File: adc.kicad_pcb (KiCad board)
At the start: 2 copper layers, 53.8 x 69.1 mm, 52 parts, among them J1 Conn_01x08_Male, J2 Conn_01x06_Male, J3 Conn_01x08_Male, J4 Conn_01x10_Male, J5 Conn_02x08_Odd_Even, J6 Conn_02x08_Odd_Even, J7 Conn_02x08_Odd_Even, U1 ADC128D818, U2 ADC128D818, U3 ADC128D818

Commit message: misc
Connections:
- J1 pad 8: 3V3 -> Net-(J1-Pad8)
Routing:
- net GND: track 32.3 -> 35.3 mm, vias 12 -> 7
- net SDA: track 70.2 -> 69.6 mm
- net Net-(R15-Pad1): track 20.2 -> 20.8 mm
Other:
- net class Default: clearance 0.2032 -> 0.1524; via_dia 0.4064 -> 0.508; via_drill 0.3556 -> 0.254
- net class Power: clearance 0.2032 -> 0.1524; via_dia 0.4064 -> 0.508; via_drill 0.3556 -> 0.254
- rule pad_to_mask_clearance: 0.051 -> 0.0508
- rule trace_clearance: 0.2032 -> 0.1524
- rule trace_min: 0.2 -> 0.1524
- rule via_min_drill: 0.3 -> 0.254
- rule via_min_size: 0.4 -> 0.508
- board text added: "0"
- board text added: "1"
- board text added: "2"
- board text added: "3"
- board text added: "4"
- board text added: "5"
- board text added: "6"
- board text added: "7"

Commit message: misc cleanup
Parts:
- moved R4 1.76 mm to (90.0, 73.2)
- moved R6 1.27 mm to (90.0, 76.8)
- moved R7 0.76 mm to (90.0, 80.5)
- moved R8 0.25 mm to (90.0, 84.2)
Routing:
- net 3V3: track 313.9 -> 317.6 mm
- net Net-(J5-Pad1): track 29.7 -> 32.1 mm
- net Net-(J5-Pad5): track 31.9 -> 34.3 mm
- net Net-(J5-Pad3): track 31.4 -> 33.5 mm
- net Net-(J7-Pad5): track 30.8 -> 32.2 mm
- net Net-(J7-Pad1): track 28.8 -> 30.1 mm
- net Net-(J6-Pad15): track 39.1 -> 40.3 mm
- net Net-(J5-Pad7): track 33.1 -> 34.2 mm
- net Net-(J6-Pad1): track 27.6 -> 28.7 mm
- net Net-(J7-Pad3): track 29.5 -> 30.3 mm
- net Net-(J5-Pad11): track 36.3 -> 35.7 mm
- net Net-(J6-Pad3): track 28.6 -> 29.3 mm
- net Net-(J6-Pad5): track 30.2 -> 30.8 mm

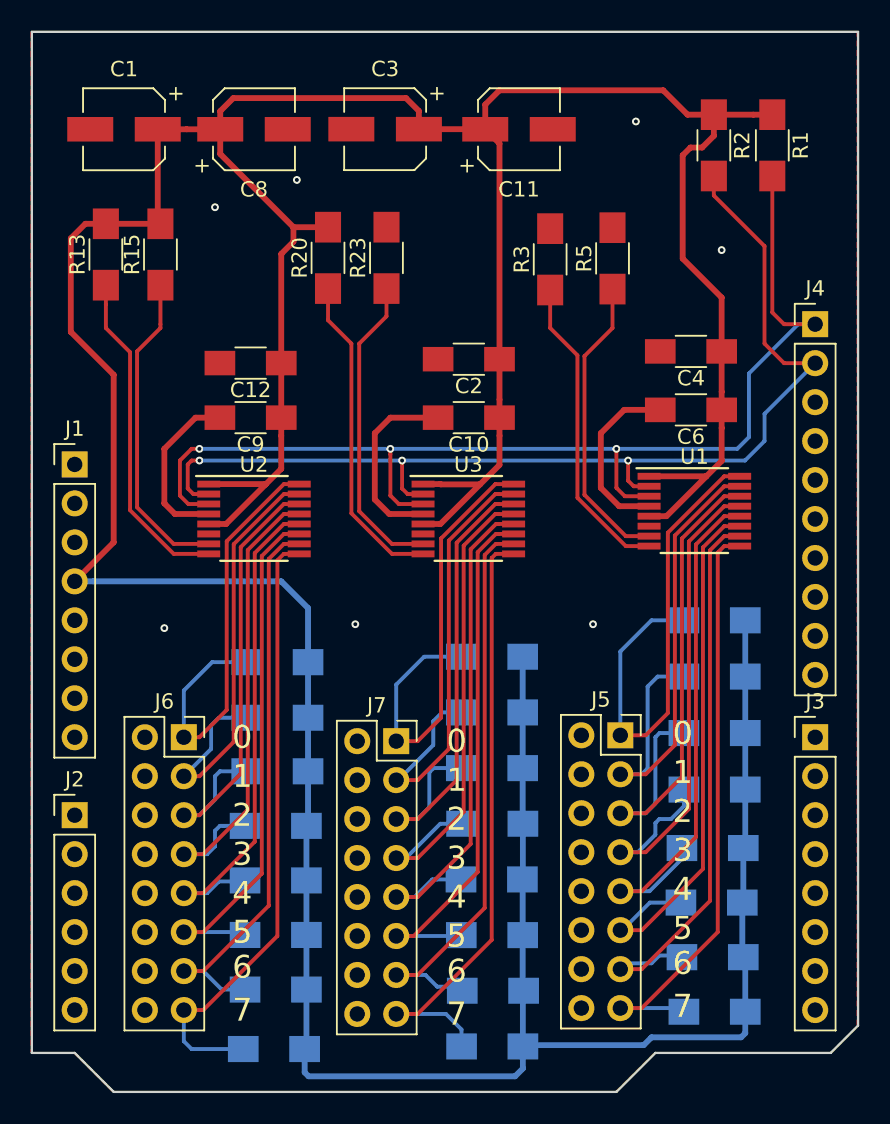
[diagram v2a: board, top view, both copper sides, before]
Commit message: reduce the number of electrolytic capacitors, improve routing
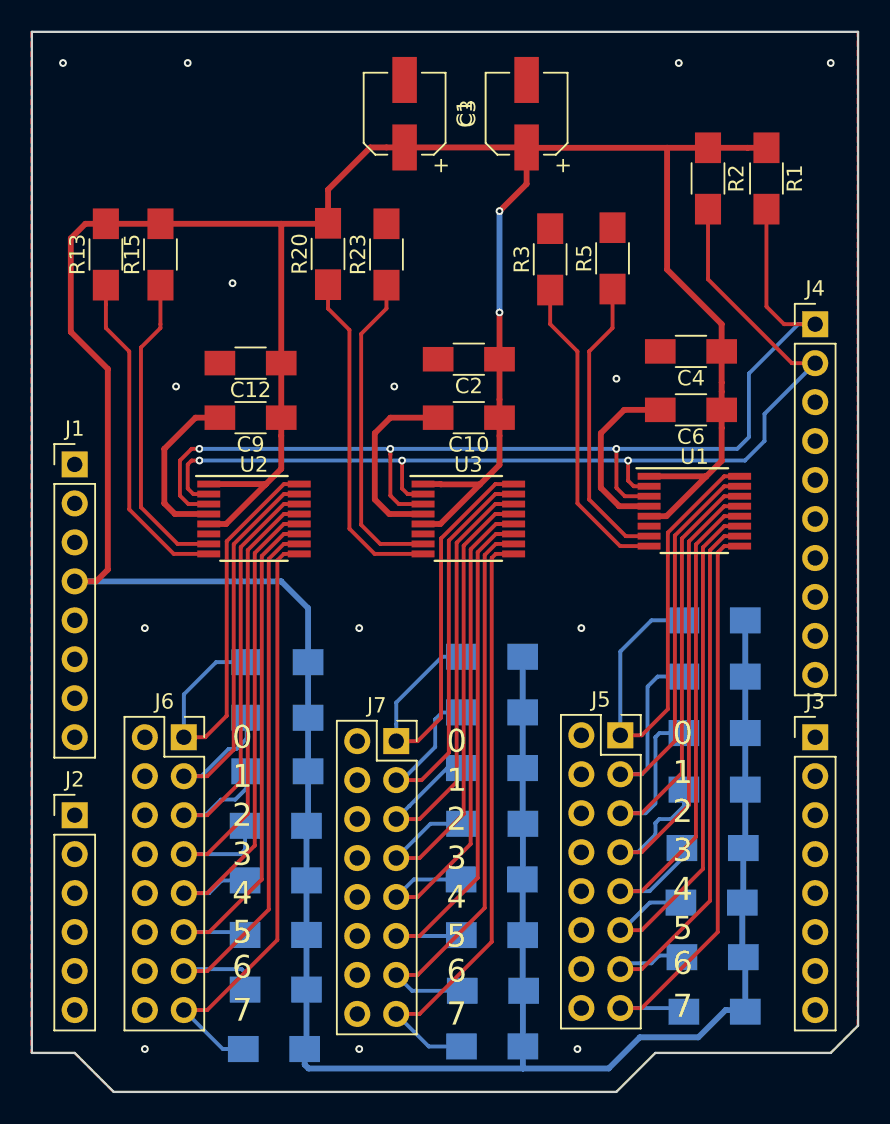
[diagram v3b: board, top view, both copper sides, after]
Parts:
- removed C11, C8: 1U ELEC, Capacitors_SMD:CP_Elec_5x5.8
- moved C1 18.3 mm to (69.8, 40.1), turned to 90 degrees
- moved C3 9.27 mm to (77.7, 40.1), turned to 90 degrees
- moved R1 2.19 mm to (93.3, 44.4)
- moved R2 2.19 mm to (89.5, 44.4)
- moved R20 0.25 mm to (64.8, 49.3)
- moved R23 0.22 mm to (68.6, 49.3)
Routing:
- net 3V3: track 317.6 -> 293.5 mm, vias 0 -> 2
- net SDA: track 70.0 -> 67.7 mm
- net SCL: track 74.2 -> 72.2 mm
- net Net-(J7-Pad5): track 32.2 -> 30.9 mm
- net Net-(J6-Pad15): track 40.3 -> 39.3 mm
- net Net-(R20-Pad1): track 21.0 -> 22.0 mm
- net Net-(J6-Pad13): track 36.8 -> 37.7 mm
- net Net-(J7-Pad1): track 30.1 -> 29.4 mm
- net Net-(J7-Pad15): track 40.4 -> 39.9 mm
- net Net-(R23-Pad1): track 20.3 -> 20.9 mm
- net GND: vias 7 -> 14
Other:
- board text added: "10K Thermistor ADC Board Rev 1 Jacob Killelea"

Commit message: change electrolytics to caps, ceramics 1206 -> 1210
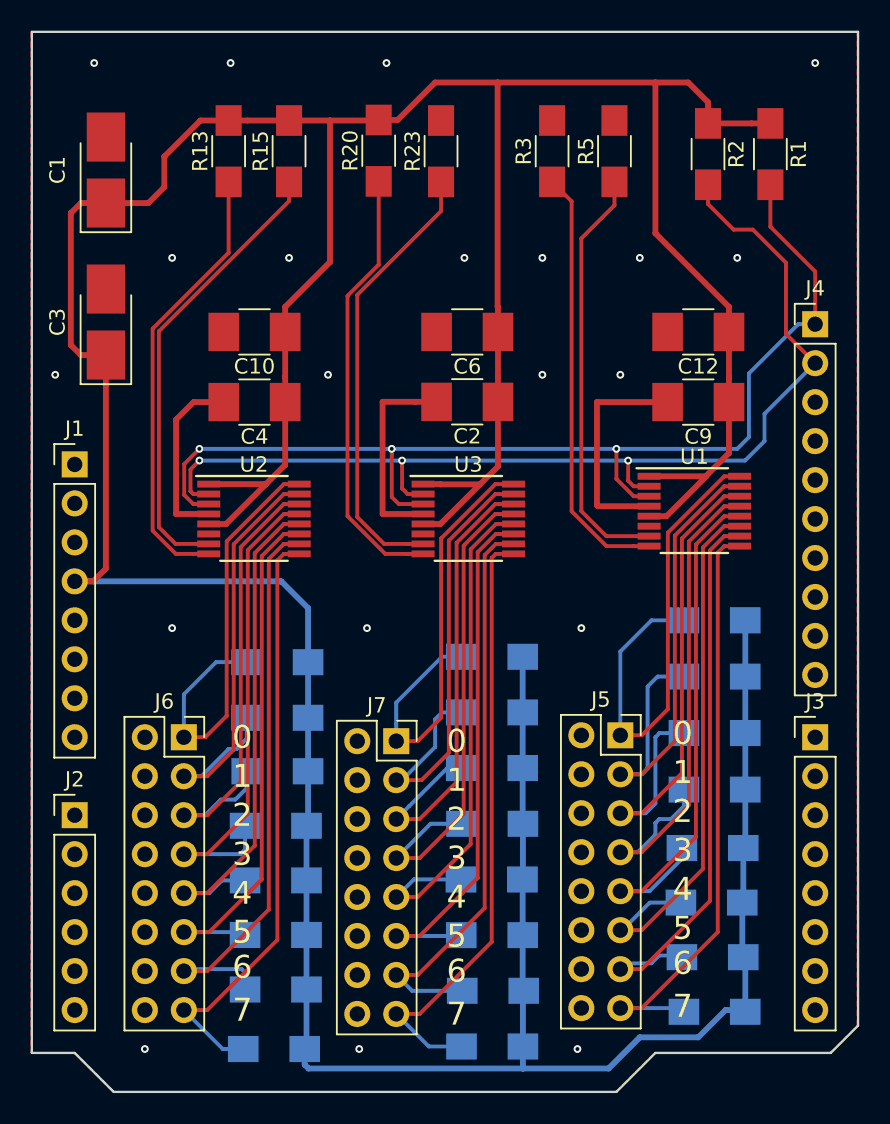
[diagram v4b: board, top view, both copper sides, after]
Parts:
- C1, C3: value 1U ELEC -> 1U TANT B; footprint Capacitors_SMD:CP_Elec_5x5.8 -> Capacitors_Tantalum_SMD:CP_Tantalum_Case-B_EIA-3528-21_Hand
- C10, C12, C2, C4, C6, C9: footprint Capacitors_SMD:C_1206_HandSoldering -> Capacitors_SMD:C_1210_HandSoldering
- moved C3 30.6 mm to (50.3, 53.7)
- moved C12 29.2 mm to (88.9, 54.4)
- moved C9 29.2 mm to (88.9, 58.9)
- moved C4 28.6 mm to (60.0, 58.9)
- moved C1 19.8 mm to (50.3, 43.8)
- moved C6 15.4 mm to (73.8, 54.4)
- moved C10 15.0 mm to (60.0, 54.4)
- moved R15 10.8 mm to (62.2, 42.6)
- moved R13 10.5 mm to (58.3, 42.6)
- moved R23 7.61 mm to (72.1, 42.6)
- moved R20 7.50 mm to (68.1, 42.5)
- moved R3 7.05 mm to (79.4, 42.6)
- moved R5 6.99 mm to (83.4, 42.6)
- moved C2 2.78 mm to (73.8, 58.9)
- moved R1 1.61 mm to (93.6, 42.8)
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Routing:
- net 3V3: track 293.5 -> 315.4 mm, vias 2 -> 0
- net Net-(R15-Pad1): track 20.4 -> 29.7 mm
- net Net-(R23-Pad1): track 20.9 -> 29.1 mm
- net Net-(R5-Pad1): track 19.2 -> 27.4 mm
- net Net-(R3-Pad1): track 20.5 -> 28.0 mm
- net Net-(R13-Pad1): track 21.6 -> 29.1 mm
- net Net-(R20-Pad1): track 22.0 -> 28.6 mm
- net GND: track 35.3 -> 40.1 mm, vias 14 -> 20
- net SDA: track 67.7 -> 68.7 mm
- net SCL: track 72.2 -> 71.4 mm

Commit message: misc
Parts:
- R10, R11, R12, R14, R16, R17, R18, R19, R21, R24, R25, R26, R27, R28, R29, R30, R31, R32, R4, R6, R7, R8, R9: value R -> 18K
- R22: value R -> 18k
- moved J7 0.34 mm to (69.5, 80.9)
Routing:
- net 3V3: track 315.4 -> 319.4 mm
- net GND: track 40.1 -> 42.3 mm
- net Net-(J6-Pad15): track 39.3 -> 40.3 mm
- net SDA: track 68.7 -> 67.9 mm
- net Net-(J7-Pad11): track 35.2 -> 34.5 mm
- net Net-(J7-Pad5): track 30.9 -> 31.6 mm
- net Net-(J6-Pad13): track 37.7 -> 38.3 mm
- net Net-(J5-Pad11): track 35.7 -> 36.2 mm
- net Net-(J7-Pad9): track 33.7 -> 33.1 mm
